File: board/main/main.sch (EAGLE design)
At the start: 42 parts, among them IC1 78m05, J1 188275-8, U2 6N138M

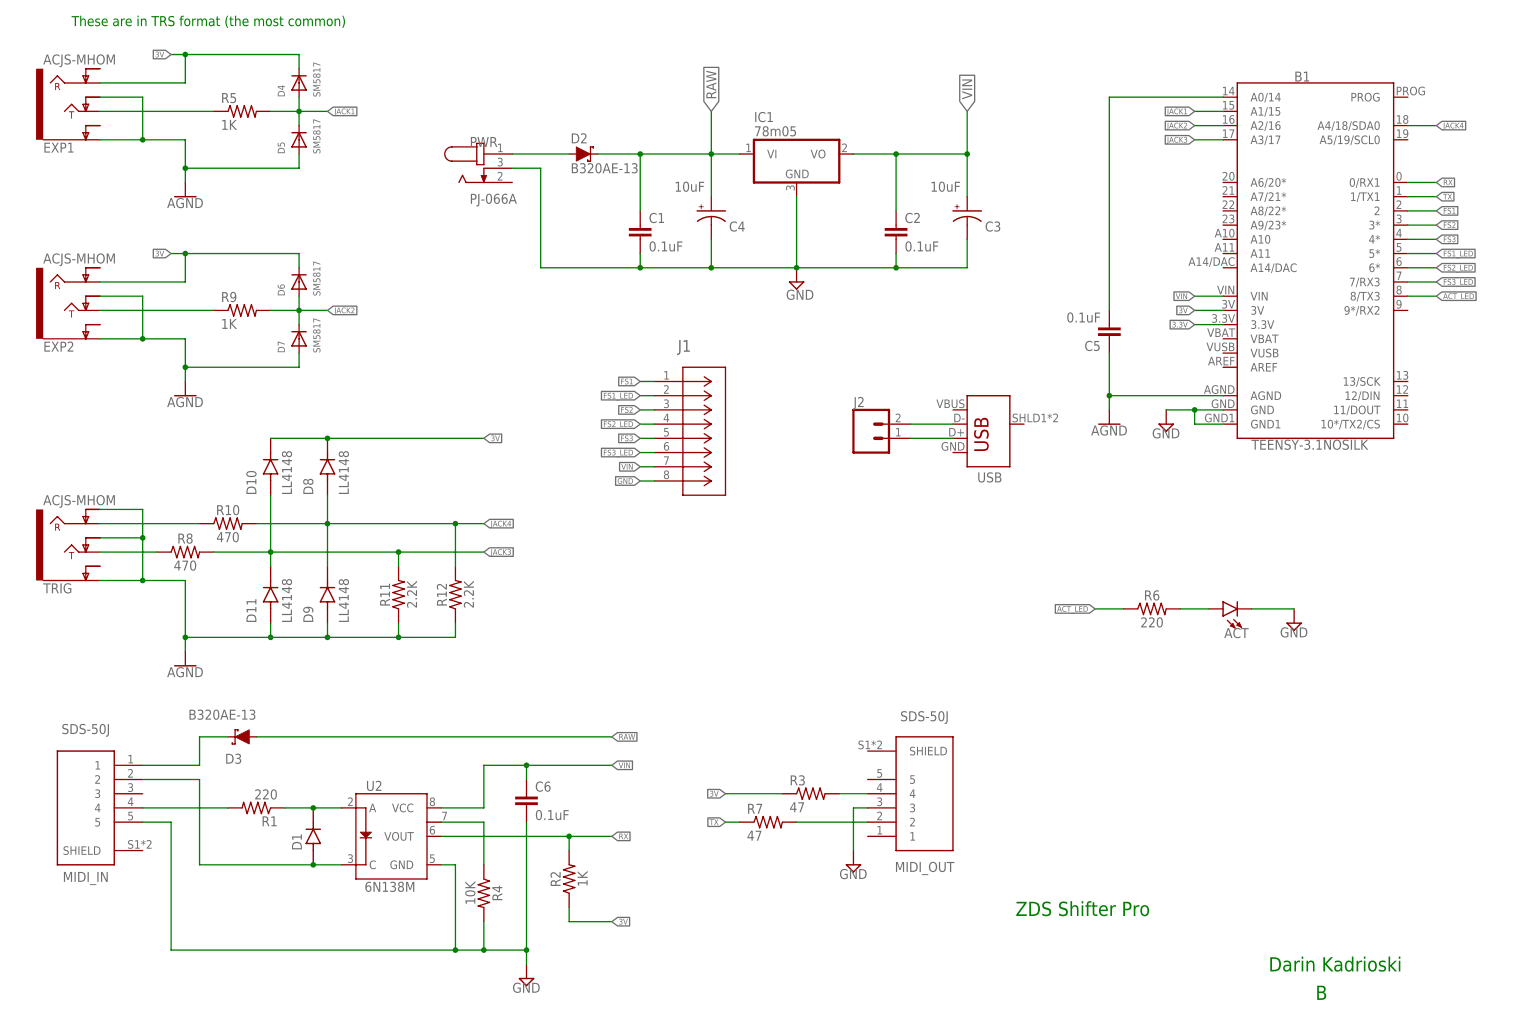
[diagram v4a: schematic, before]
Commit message: refactoring board
moving to stacked 1/4 jacks to reduce board width
switching to resistor networks and diode arrays to shrink footprint and make assembly a bit easier
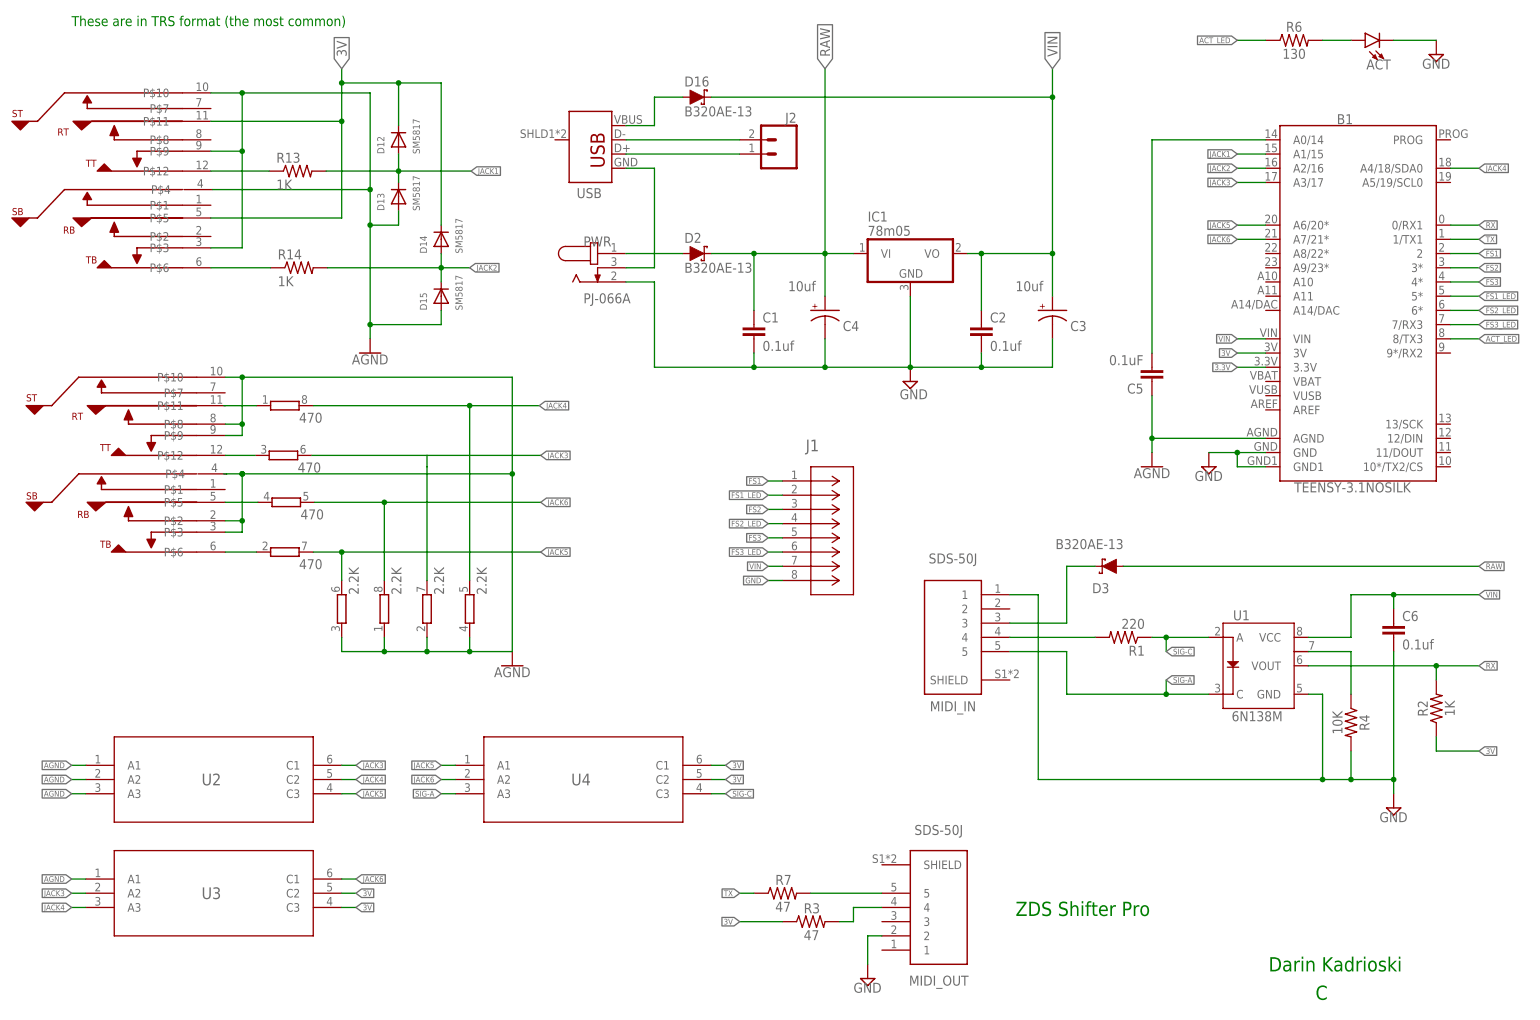
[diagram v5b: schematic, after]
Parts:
- removed D1: S3M, LL4148:LL4148
- removed D10, D11, D8, D9: LL4148, LL4148:LL4148
- removed D4, D5, D6, D7: SM5817, adafruit:DIODE_SOD-123FL
- removed EXP1, EXP2, TRIG: ACJS-MHOM, ACJS-MHOM:ACJS-MHOM
- removed R10, R8: 470, SparkFun-Resistors:RESISTOR1206
- removed R11, R12: 2.2K, SparkFun-Resistors:RESISTOR1206
- removed R5, R9: 1K, SparkFun-Resistors:RESISTOR1206
- added D12, D13, D14, D15: SM5817, adafruit:DIODE_SOD-123FL
- added D16: B320AE-13, SparkFun-DiscreteSemi:DIODE-SCHOTTKY-SS14
- added EXP: EXP, ACJS-MHDCM:ACJS-MHDCM
- added R13, R14: 1K, SparkFun-Resistors:RESISTOR1206
- added RN1: 470, resistor-dil:4R-NEXB38V
- added RN2: 2.2K, resistor-dil:4R-NEXB38V
- added TRIG1: TRIG, ACJS-MHDCM:ACJS-MHDCM
- added U1: 6N138M, darin-custom:OPTO_DARL_6N138S
- added U3, U4: MMBD4148TW-7-F, MMBD4148TW7F:MMBD4148TW-7-F
- C1, C2, C6: value 0.1uF -> 0.1uf
- C3, C4: value 10uF -> 10uf
- R6: value 220 -> 130
- U2: value 6N138M -> MMBD4148TW-7-F; device darin-custom:OPTO_DARL_6N138S -> MMBD4148TW7F:MMBD4148TW-7-F
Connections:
- removed net N$14: EXP1.TIP, R5.1
- removed net N$6 (its old number): MIDI_OUT.2, R7.2
- new net JACK5: B1.A6/20*, RN1B.2, RN2C.2, U2.C3, U4.A1
- new net JACK6: B1.A7/21*, RN1D.2, RN2A.2, U3.C1, U4.A2
- new net N$15: PWR.3, USB.GND
- new net N$17: D16.A, USB.VBUS
- new net N$18: EXP.P$12, R13.1
- new net N$21: EXP.P$6, R14.1
- new net N$8: MIDI_OUT.5, R7.2
- new net SIG-A: MIDI_IN.5, U1.C, U4.A3
- new net SIG-C: R1.1, U1.A, U4.C3
- net 3V: now also D12.C, D14.C, EXP.P$11, EXP.P$5, U3.C2, U3.C3, U4.C1, U4.C2; no longer D10.C, D4.C, D6.C, D8.C, EXP1.RING, EXP2.RING
- net AGND: now also D13.A, D15.A, EXP.P$10, EXP.P$3, EXP.P$4, EXP.P$9, RN2A.1, RN2B.1, RN2C.1, RN2D.1, TRIG1.P$10, TRIG1.P$2, TRIG1.P$3, TRIG1.P$4, TRIG1.P$8, TRIG1.P$9, U2.A1, U2.A2, U2.A3, U3.A1; no longer D11.A, D5.A, D7.A, D9.A, EXP1.EARTH, EXP1.TIP-NORM, EXP2.EARTH, EXP2.TIP-NORM, R11.1, R12.1, TRIG.EARTH, TRIG.RING-NORM, TRIG.TIP-NORM
- net GND: now also MIDI_IN.1, MIDI_OUT.2, PWR.2, U1.GND; no longer MIDI_IN.5, MIDI_OUT.3, PWR.3, U2.GND
- net JACK1: now also D12.A, D13.C, R13.2; no longer D4.A, D5.C, R5.2
- net JACK2: now also D14.A, D15.C, R14.2; no longer D6.A, D7.C, R9.2
- net JACK3: now also RN1C.2, RN2B.2, U2.C1, U3.A2; no longer D10.A, D11.C, R11.2, R8.1, R8.2, TRIG.TIP
- net JACK4: now also RN1A.2, RN2D.2, U2.C2, U3.A3; no longer D8.A, D9.C, R10.2, R12.2
- net N$11: now also U1.7; no longer U2.7
- net N$12: now also RN1C.1, TRIG1.P$12; no longer R10.1, TRIG.RING
- net N$16: now also RN1A.1, TRIG1.P$11; no longer D1.C, R1.1, U2.A
- net N$2: now also RN1B.1, TRIG1.P$6; no longer D1.A, MIDI_IN.2, U2.C
- net N$5: now also MIDI_IN.3; no longer MIDI_IN.1
- net N$9: now also RN1D.1, TRIG1.P$5; no longer EXP2.TIP, R9.1
- net RX: now also U1.VOUT; no longer U2.VOUT
- net VIN: now also D16.C, U1.VCC; no longer U2.VCC
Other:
- moved on the sheet: ACT, B1, C1, C2, C3, C4, C5, C6, D2, D3, IC1, J1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

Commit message: submitted REV C of the main board for manufacture
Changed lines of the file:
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@@
 <wire x1="60.706" y1="103.632" x2="81.28" y2="103.632" width="0.1524" layer="91"/>
 <wire x1="81.28" y1="103.632" x2="81.28" y2="101.6" width="0.1524" layer="91"/>
+<junction x="81.28" y="103.632"/>
 </segment>
 <segment>
@@
 <pinref part="U$2" gate="G$1" pin="AGND"/>
 <wire x1="96.52" y1="100.33" x2="96.52" y2="68.58" width="0.1524" layer="91"/>
-<wire x1="96.52" y1="68.58" x2="88.9" y2="68.58" width="0.1524" layer="91"/>
 <pinref part="TRIG1" gate="G$1" pin="P$4"/>
-<wire x1="88.9" y1="68.58" x2="81.28" y2="68.58" width="0.1524" layer="91"/>
-<wire x1="81.28" y1="68.58" x2="73.66" y2="68.58" width="0.1524" layer="91"/>
-<wire x1="73.66" y1="68.58" x2="66.04" y2="68.58" width="0.1524" layer="91"/>
-<wire x1="45.466" y1="100.33" x2="44.958" y2="100.33" width="0.1524" layer="91"/>
 <wire x1="45.466" y1="100.33" x2="48.26" y2="100.33" width="0.1524" layer="91"/>
 <junction x="96.52" y="100.33"/>
@@
 <junction x="48.26" y="91.948"/>
 <wire x1="48.26" y1="91.948" x2="48.26" y2="100.33" width="0.1524" layer="91"/>
-<pinref part="RN2" gate="C" pin="1"/>
-<wire x1="66.04" y1="71.12" x2="66.04" y2="68.58" width="0.1524" layer="91"/>
+<pinref part="RN2" gate="D" pin="1"/>
+<wire x1="88.9" y1="71.12" x2="88.9" y2="68.58" width="0.1524" layer="91"/>
+<wire x1="88.9" y1="68.58" x2="81.28" y2="68.58" width="0.1524" layer="91"/>
+<pinref part="RN2" gate="B" pin="1"/>
+<wire x1="81.28" y1="71.12" x2="81.28" y2="68.58" width="0.1524" layer="91"/>
+<junction x="81.28" y="68.58"/>
+<wire x1="81.28" y1="68.58" x2="73.66" y2="68.58" width="0.1524" layer="91"/>
 <pinref part="RN2" gate="A" pin="1"/>
 <wire x1="73.66" y1="71.12" x2="73.66" y2="68.58" width="0.1524" layer="91"/>
 <junction x="73.66" y="68.58"/>
-<pinref part="RN2" gate="B" pin="1"/>
-<wire x1="81.28" y1="71.12" x2="81.28" y2="68.58" width="0.1524" layer="91"/>
-<junction x="81.28" y="68.58"/>
-<pinref part="RN2" gate="D" pin="1"/>
-<wire x1="88.9" y1="71.12" x2="88.9" y2="68.58" width="0.1524" layer="91"/>
+<wire x1="73.66" y1="68.58" x2="66.04" y2="68.58" width="0.1524" layer="91"/>
+<pinref part="RN2" gate="C" pin="1"/>
+<wire x1="66.04" y1="71.12" x2="66.04" y2="68.58" width="0.1524" layer="91"/>
+<wire x1="88.9" y1="68.58" x2="96.52" y2="68.58" width="0.1524" layer="91"/>
 <junction x="88.9" y="68.58"/>
+<junction x="96.52" y="68.58"/>
 </segment>
 <segment>
@@
 <segment>
 <pinref part="TRIG1" gate="G$1" pin="P$11"/>
-<wire x1="45.212" y1="112.522" x2="44.958" y2="112.522" width="0.1524" layer="91"/>
 <pinref part="RN1" gate="A" pin="1"/>
 <wire x1="45.212" y1="112.522" x2="50.8" y2="112.522" width="0.1524" layer="91"/>

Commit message: board changes
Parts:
- added R5, R8: 100, SparkFun-Resistors:RESISTOR1206
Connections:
- new net N$14: EXP.P$11, R5.1
- new net N$19: EXP.P$5, R8.1
- net 3V: now also R5.2, R8.2; no longer EXP.P$11, EXP.P$5
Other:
- note added: "Signal diodes"
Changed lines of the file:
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@@
 <attributes>
 <attribute name="CNAME" value="ZDS Shifter Pro"/>
-<attribute name="CREVISION" value="C"/>
+<attribute name="CREVISION" value="D"/>
 <attribute name="DESIGNER" value="Darin Kadrioski"/>
 </attributes>
@@
 <part name="RN1" library="resistor-dil" deviceset="4R-N" device="EXB38V" value="470"/>
 <part name="RN2" library="resistor-dil" deviceset="4R-N" device="EXB38V" value="2.2K"/>
+<part name="R5" library="SparkFun-Resistors" library_urn="urn:adsk.eagle:library:532" deviceset="RESISTOR" device="1206" package3d_urn="urn:adsk.eagle:package:39654/1" value="100"/>
+<part name="R8" library="SparkFun-Resistors" library_urn="urn:adsk.eagle:library:532" deviceset="RESISTOR" device="1206" package3d_urn="urn:adsk.eagle:package:39654/1" value="100"/>
 </parts>
 <sheets>
@@
 <text x="231.648" y="11.43" size="2.54" layer="91">&gt;DESIGNER</text>
 <text x="240.03" y="6.35" size="2.54" layer="91">&gt;CREVISION</text>
+<text x="35.56" y="58.42" size="1.778" layer="91">Signal diodes</text>
 </plain>
 <instances>
@@
 <instance part="RN2" gate="D" x="88.9" y="76.2" smashed="yes" rot="R90">
 <attribute name="VALUE" x="91.948" y="78.74" size="1.778" layer="96" rot="R90"/>
+</instance>
+<instance part="R5" gate="G$1" x="57.658" y="163.322" smashed="yes">
+<attribute name="NAME" x="53.848" y="164.8206" size="1.778" layer="95"/>
+<attribute name="VALUE" x="53.848" y="160.02" size="1.778" layer="96"/>
+</instance>
+<instance part="R8" gate="G$1" x="58.42" y="146.05" smashed="yes">
+<attribute name="NAME" x="54.61" y="147.5486" size="1.778" layer="95"/>
+<attribute name="VALUE" x="54.61" y="142.748" size="1.778" layer="96"/>
 </instance>
 </instances>
@@
 <wire x1="66.04" y1="172.72" x2="66.04" y2="170.18" width="0.1524" layer="91"/>
 <label x="66.04" y="172.72" size="1.778" layer="95" rot="R90" xref="yes"/>
-<pinref part="EXP" gate="G$1" pin="P$11"/>
 <wire x1="66.04" y1="170.18" x2="66.04" y2="163.322" width="0.1524" layer="91"/>
-<wire x1="66.04" y1="163.322" x2="42.672" y2="163.322" width="0.1524" layer="91"/>
-<pinref part="EXP" gate="G$1" pin="P$5"/>
 <wire x1="66.04" y1="163.322" x2="66.04" y2="146.05" width="0.1524" layer="91"/>
-<wire x1="66.04" y1="146.05" x2="42.672" y2="146.05" width="0.1524" layer="91"/>
 <junction x="66.04" y="163.322"/>
 <pinref part="D12" gate="G$1" pin="C"/>
@@
 <wire x1="83.82" y1="170.18" x2="76.2" y2="170.18" width="0.1524" layer="91"/>
 <junction x="76.2" y="170.18"/>
+<wire x1="66.04" y1="163.322" x2="62.738" y2="163.322" width="0.1524" layer="91"/>
+<pinref part="R5" gate="G$1" pin="2"/>
+<wire x1="66.04" y1="146.05" x2="63.5" y2="146.05" width="0.1524" layer="91"/>
+<pinref part="R8" gate="G$1" pin="2"/>
 </segment>
 <segment>
@@
 </segment>
 </net>
+<net name="N$14" class="1">
+<segment>
+<pinref part="EXP" gate="G$1" pin="P$11"/>
+<wire x1="52.578" y1="163.322" x2="42.672" y2="163.322" width="0.1524" layer="91"/>
+<pinref part="R5" gate="G$1" pin="1"/>
+</segment>
+</net>
+<net name="N$19" class="1">
+<segment>
+<pinref part="EXP" gate="G$1" pin="P$5"/>
+<wire x1="53.34" y1="146.05" x2="42.672" y2="146.05" width="0.1524" layer="91"/>
+<pinref part="R8" gate="G$1" pin="1"/>
+</segment>
+</net>

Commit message: Main board, revision E
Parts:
- removed D12, D13, D14, D15: SM5817, adafruit:DIODE_SOD-123FL
- removed R13, R14, R2: 1K, SparkFun-Resistors:RESISTOR1206
- added RN3: 1K, resistor-dil:4R-NEXB38V
- added U5: BAT54SDW-7-F, BAT54SDW7F:BAT54SDW-7-F
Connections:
- net 3V: now also RN3C.1, U5.C1, U5.C2; no longer D12.C, D14.C, R2.1
- net AGND: now also U5.A1, U5.A2; no longer D13.A, D15.A
- net JACK1: now also RN3A.2, U5.AC1; no longer D12.A, D13.C, R13.2
- net JACK2: now also RN3B.2, U5.AC2; no longer D14.A, D15.C, R14.2
- net N$18: now also RN3A.1; no longer R13.1
- net N$21: now also RN3B.1; no longer R14.1
- net RX: now also RN3C.2; no longer R2.2
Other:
- note added: "Schottky diodes"
- note added: "Signal diodes (U2-4)"
- note removed: "Signal diodes"
- moved on the sheet: ACT, B1, C5, C6, D3, J1, MIDI_IN, MIDI_OUT, R1, R3, R4, R6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
